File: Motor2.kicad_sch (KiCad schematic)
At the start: 53 parts, among them J601 Step Out, J604 Direction, J605 Direction, Q601 WSF07N10, Q602 WSF07N10, Q603 WSF07N10, Q604 WSF07N10, Q605 WSF07N10, Q606 WSF07N10, Q607 WSF07N10, Q608 WSF07N10

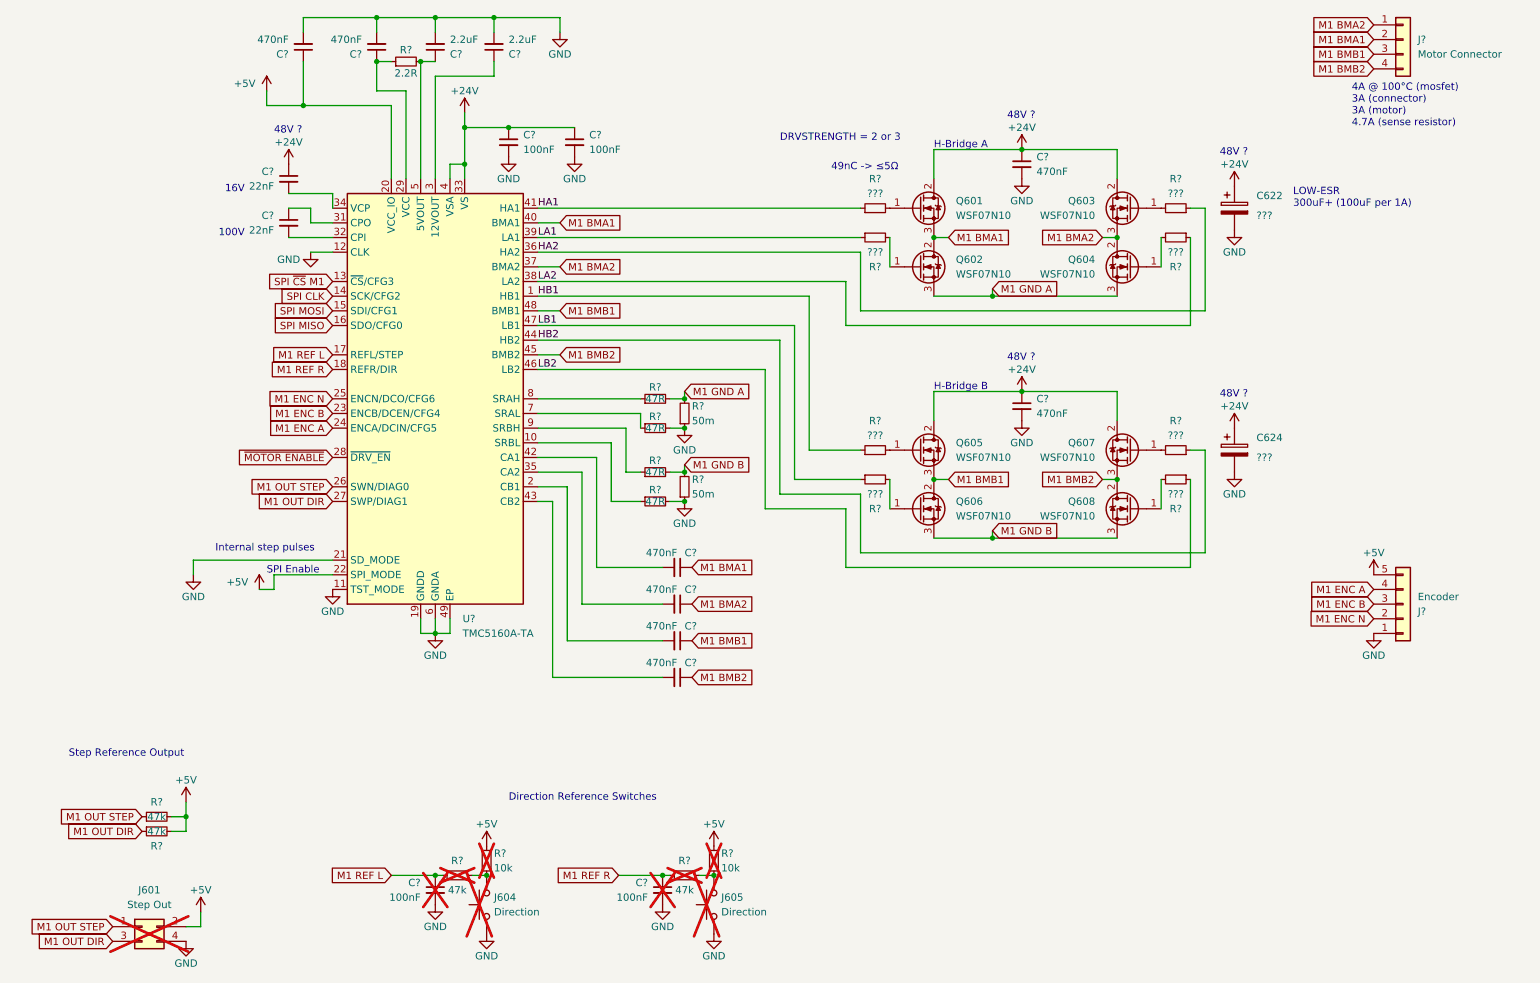
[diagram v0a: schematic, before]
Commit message: Assigning a lot of values to components Change MOSFETS for different (correct) ones Copy Motor1 to Motor2-4 Guess max current per voltage on PowerSupply schema
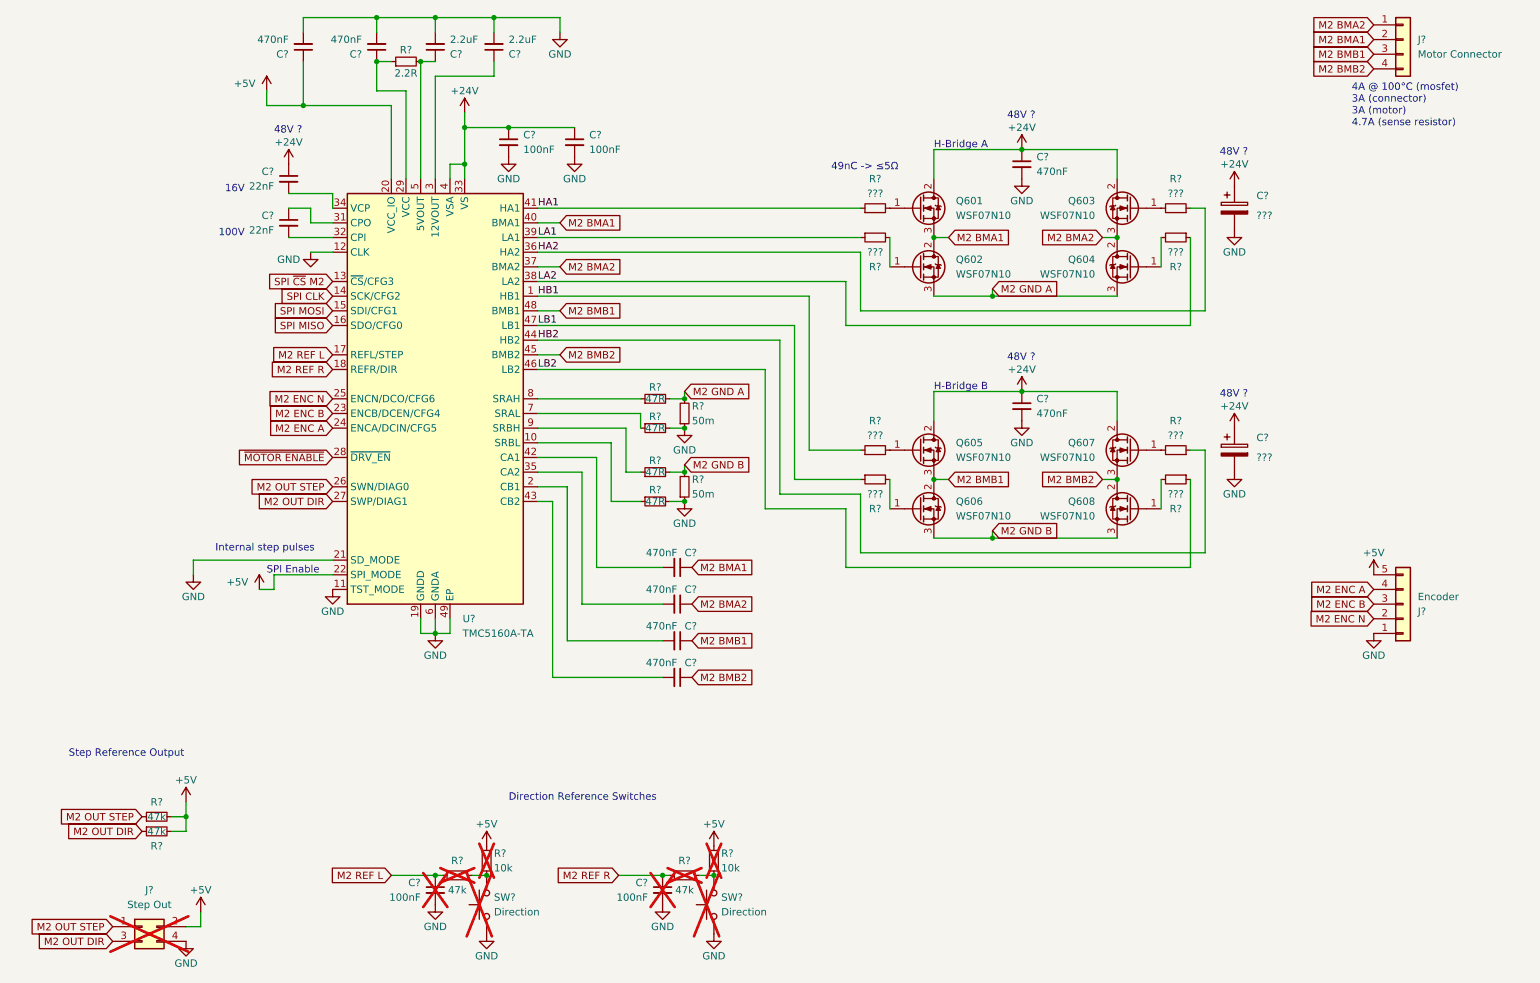
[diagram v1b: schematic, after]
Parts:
- removed C622, C624: ???, symbol Device:C_Polarized
- removed C? (x6): 470nF, Capacitor_SMD:C_1210_3225Metric, symbol Device:C_Small
- removed C? (x4): 100nF, symbol Device:C_Small
- removed C? (x2): 2.2uF, symbol Device:C_Small
- removed C? (x2): 470nF, symbol Device:C_Small
- removed C? (x2): 22nF, symbol Device:C_Small
- removed J601: Step Out, Connector_PinHeader_2.54mm:PinHeader_2x02_P2.54mm_Vertical, symbol Connector_Generic:Conn_02x02_Odd_Even
- removed J604, J605: Direction, Connector_PinHeader_2.54mm:PinHeader_1x02_P2.54mm_Vertical, symbol Switch:SW_Push
- removed J?: Encoder, Connector_JST:JST_XH_B5B-XH-A_1x05_P2.50mm_Vertical, symbol Connector_Generic:Conn_01x05
- removed J?: Motor Connector, Connector_JST:JST_XH_B4B-XH-A_1x04_P2.50mm_Vertical, symbol Connector_Generic:Conn_01x04
- removed R? (x2): 50m, Resistor_SMD:R_2512_6332Metric, symbol Device:R_Small
- removed R? (x4): 47k, symbol Device:R_Small
- removed R? (x8): ???, symbol Device:R_Small
- removed R? (x4): 47R, symbol Device:R_Small
- removed R?: 2.2R, symbol Device:R_Small
- removed R? (x2): 10k, symbol Device:R_Small
- removed U?: TMC5160A-TA, Package_QFP:TQFP-48-1EP_7x7mm_P0.5mm_EP5x5mm_ThermalVias, symbol Driver_Motor:TMC5160A-TA
- added C? (x6): 470nF, Capacitor_SMD:C_1210_3225Metric, symbol Device:C_Small
- added C? (x4): 100nF, symbol Device:C_Small
- added C? (x2): 470nF, symbol Device:C_Small
- added C? (x2): ???, symbol Device:C_Polarized
- added C? (x2): 22nF, symbol Device:C_Small
- added C? (x2): 2.2uF, symbol Device:C_Small
- added J?: Step Out, Connector_PinHeader_2.54mm:PinHeader_2x02_P2.54mm_Vertical, symbol Connector_Generic:Conn_02x02_Odd_Even
- added J?: Motor Connector, Connector_JST:JST_XH_B4B-XH-A_1x04_P2.50mm_Vertical, symbol Connector_Generic:Conn_01x04
- added J?: Encoder, Connector_JST:JST_XH_B5B-XH-A_1x05_P2.50mm_Vertical, symbol Connector_Generic:Conn_01x05
- added R? (x2): 10k, symbol Device:R_Small
- added R? (x4): 47k, symbol Device:R_Small
- added R? (x4): 47R, symbol Device:R_Small
- added R? (x8): ???, symbol Device:R_Small
- added R? (x2): 50m, Resistor_SMD:R_2512_6332Metric, symbol Device:R_Small
- added R?: 2.2R, symbol Device:R_Small
- added SW? (x2): Direction, Connector_PinHeader_2.54mm:PinHeader_1x02_P2.54mm_Vertical, symbol Switch:SW_Push
- added U?: TMC5160A-TA, Package_QFP:TQFP-48-1EP_7x7mm_P0.5mm_EP5x5mm_ThermalVias, symbol Driver_Motor:TMC5160A-TA
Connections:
- net +24V: now also C?.1, C?.1, C?.1, C?.1, C?.1, C?.1, C?.1, U?.33 (VS), U?.4 (VSA)
- net +5V: now also C?.1, J?.2 (Pin_2), J?.5 (Pin_5), R?.2, R?.2, R?.2, R?.2, U?.20 (VCC_IO), U?.22 (SPI_MODE)
- net GND: now also C?.2, C?.2, C?.2, C?.2, C?.2, C?.2, C?.2, C?.2, C?.2, C?.2, C?.2, C?.2, J?.1 (Pin_1), J?.4 (Pin_4), R?.1, R?.1, R?.2, R?.2, SW?.1, SW?.1, U?.11 (TST_MODE), U?.12 (CLK), U?.19 (GNDD), U?.21 (SD_MODE), U?.30 (GNDD), U?.49 (EP), U?.6 (GNDA)
- net HA1: now also R?.1, U?.41 (HA1)
- net HA2: now also R?.1, U?.36 (HA2)
- net HB1: now also R?.1, U?.1 (HB1)
- net HB2: now also R?.1, U?.44 (HB2)
- net LA1: now also R?.1, U?.39 (LA1)
- net LA2: now also R?.1, U?.38 (LA2)
- net LB1: now also R?.1, U?.47 (LB1)
- net LB2: now also R?.1, U?.46 (LB2)
- net SPI CLK: now also U?.14 (SCK/CFG2)
- net SPI MISO: now also U?.16 (SDO/CFG0)
- net SPI MOSI: now also U?.15 (SDI/CFG1)
- net ~{MOTOR ENABLE}: now also U?.28 (~{DRV_EN})
- net at Q606.1 (G): now also R?.2
- net at Q602.1 (G): now also R?.2
- net at Q608.1 (G): now also R?.2
- net at Q601.1 (G): now also R?.2
- net at Q607.1 (G): now also R?.2
- net at Q603.1 (G): now also R?.2
- net at Q605.1 (G): now also R?.2
- net at Q604.1 (G): now also R?.2
- net M1 BMA1 renamed M2 BMA1
- net M2 BMA1: now also C?.1, J?.2 (Pin_2), U?.40 (BMA1)
- net M1 BMA2 renamed M2 BMA2
- net M2 BMA2: now also C?.1, J?.1 (Pin_1), U?.37 (BMA2)
- net M1 BMB1 renamed M2 BMB1
- net M2 BMB1: now also C?.1, J?.3 (Pin_3), U?.48 (BMB1)
- net M1 BMB2 renamed M2 BMB2
- net M2 BMB2: now also C?.1, J?.4 (Pin_4), U?.45 (BMB2)
- net M1 GND A renamed M2 GND A
- net M2 GND A: now also R?.2, R?.2
- net M1 GND B renamed M2 GND B
- net M2 GND B: now also R?.2, R?.2
- new net: R?.1, R?.2, SW?.2 (x2)
- new net: R?.1, U?.7 (SRAL)
- new net: C?.2, U?.42 (CA1)
- new net: C?.2, U?.43 (CB2)
- new net: C?.1, R?.1, U?.29 (VCC)
- new net: C?.1, U?.31 (CPO)
- new net: C?.2, U?.32 (CPI)
- new net: R?.1, U?.9 (SRBH)
- new net: R?.1, U?.10 (SRBL)
- new net: C?.2, U?.2 (CB1)
- new net: C?.1, U?.3 (12VOUT)
- new net: C?.2, U?.34 (VCP)
- new net: C?.2, U?.35 (CA2)
- new net: C?.1, R?.2, U?.5 (5VOUT)
- new net: R?.1, U?.8 (SRAH)
- new net M2 ENC A: J?.4 (Pin_4), U?.24 (ENCA/DCIN/CFG5)
- new net M2 ENC B: J?.3 (Pin_3), U?.23 (ENCB/DCEN/CFG4)
- new net M2 ENC N: J?.2 (Pin_2), U?.25 (ENCN/DCO/CFG6)
- new net M2 OUT DIR: J?.3 (Pin_3), R?.1, U?.27 (SWP/DIAG1)
- new net M2 OUT STEP: J?.1 (Pin_1), R?.1, U?.26 (SWN/DIAG0)
- new net M2 REF L: C?.1, R?.1, U?.17 (REFL/STEP)
- new net M2 REF R: C?.1, R?.1, U?.18 (REFR/DIR)
- new net SPI ~{CS} M2: U?.13 (~{CS}/CFG3)
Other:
- note removed: "DRVSTRENGTH = 2 or 3"
- note removed: "LOW-ESR 300uF+ (100uF per 1A)"
- title: CAN 3D Printer (4 Motor) - Motor 1 -> CAN 3D Printer (4 Motor) - Motor 2

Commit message: Complete schematics Assign every value (very few exceptions) Change TCM5160 from on-board to separate module Add fuses Add power supplies (LDO + 2x buck converter)
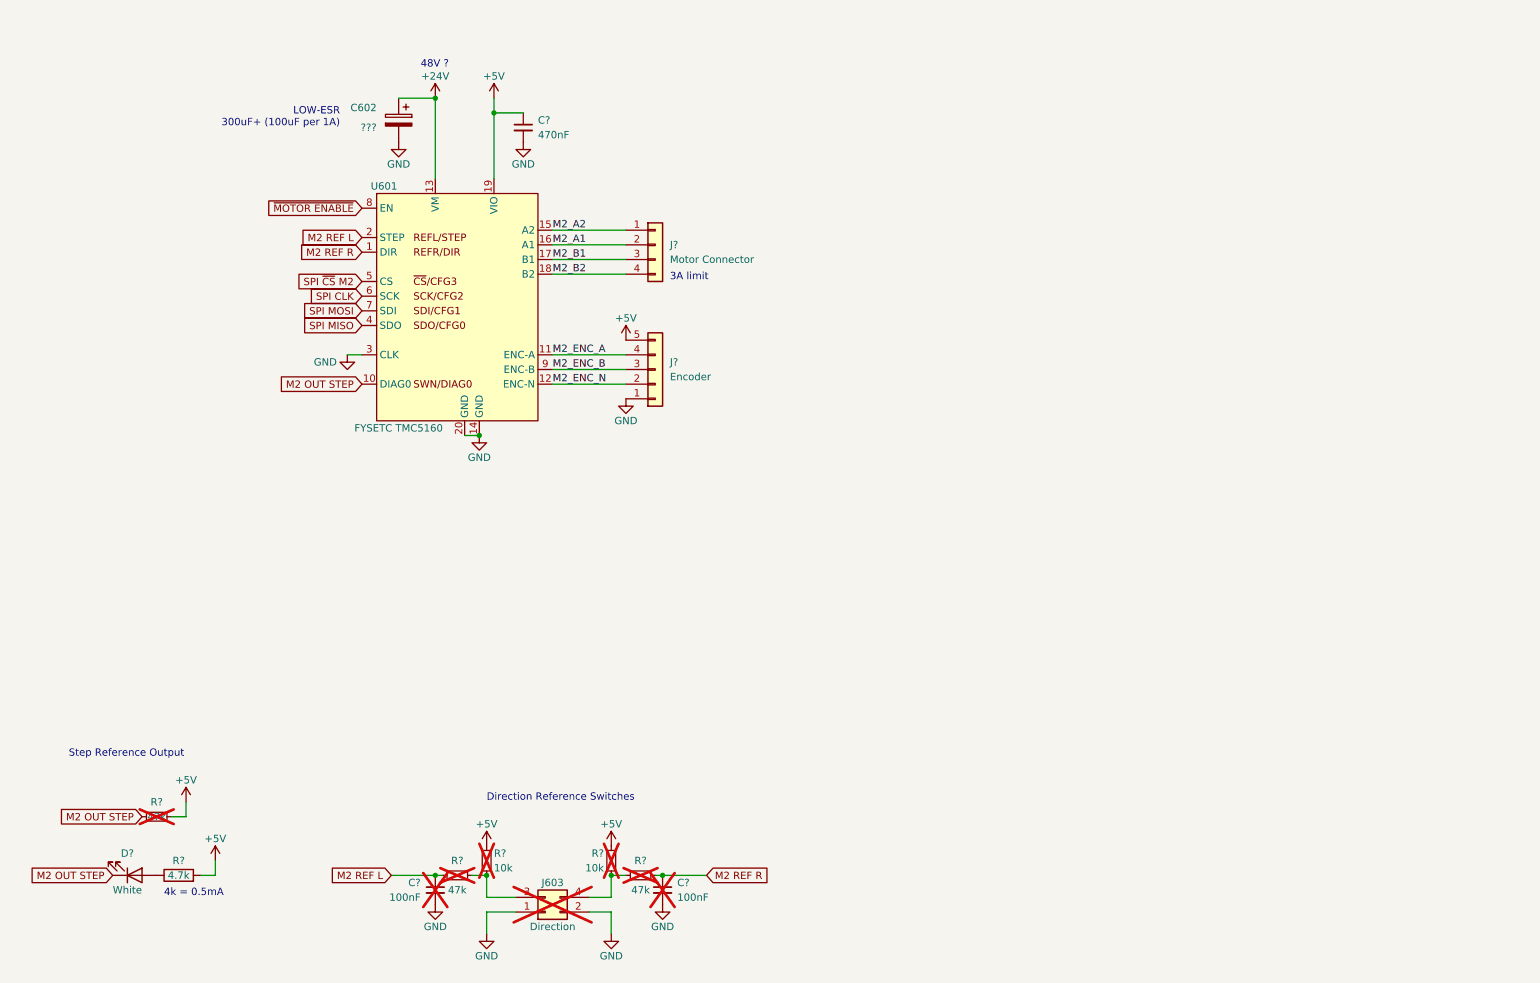
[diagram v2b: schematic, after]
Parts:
- removed C? (x6): 470nF, Capacitor_SMD:C_1210_3225Metric, symbol Device:C_Small
- removed C? (x4): 100nF, symbol Device:C_Small
- removed C? (x2): 470nF, symbol Device:C_Small
- removed C? (x2): ???, symbol Device:C_Polarized
- removed C? (x2): 22nF, symbol Device:C_Small
- removed C? (x2): 2.2uF, symbol Device:C_Small
- removed J?: Step Out, Connector_PinHeader_2.54mm:PinHeader_2x02_P2.54mm_Vertical, symbol Connector_Generic:Conn_02x02_Odd_Even
- removed J?: Motor Connector, Connector_JST:JST_XH_B4B-XH-A_1x04_P2.50mm_Vertical, symbol Connector_Generic:Conn_01x04
- removed J?: Encoder, Connector_JST:JST_XH_B5B-XH-A_1x05_P2.50mm_Vertical, symbol Connector_Generic:Conn_01x05
- removed Q601, Q602, Q603, Q604, Q605, Q606, Q607, Q608: WSF07N10, Package_TO_SOT_SMD:TO-252-2, symbol Transistor_FET:QM6006D
- removed R? (x2): 10k, symbol Device:R_Small
- removed R? (x4): 47k, symbol Device:R_Small
- removed R? (x4): 47R, symbol Device:R_Small
- removed R? (x8): ???, symbol Device:R_Small
- removed R? (x2): 50m, Resistor_SMD:R_2512_6332Metric, symbol Device:R_Small
- removed R?: 2.2R, symbol Device:R_Small
- removed SW? (x2): Direction, Connector_PinHeader_2.54mm:PinHeader_1x02_P2.54mm_Vertical, symbol Switch:SW_Push
- removed U?: TMC5160A-TA, Package_QFP:TQFP-48-1EP_7x7mm_P0.5mm_EP5x5mm_ThermalVias, symbol Driver_Motor:TMC5160A-TA
- added C602: ???, symbol Device:C_Polarized
- added C? (x2): 100nF, Capacitor_SMD:C_0402_1005Metric, symbol Device:C_Small
- added C?: 470nF, Capacitor_SMD:C_0603_1608Metric, symbol Device:C_Small
- added D?: White, LED_SMD:LED_0402_1005Metric, symbol Device:LED
- added J603: Direction, Connector_PinHeader_2.54mm:PinHeader_2x02_P2.54mm_Vertical, symbol Connector_Generic:Conn_02x02_Odd_Even
- added J?: Encoder, Connector_JST:JST_XH_B5B-XH-A_1x05_P2.50mm_Vertical, symbol Connector_Generic:Conn_01x05
- added J?: Motor Connector, Connector_JST:JST_XH_B4B-XH-A_1x04_P2.50mm_Vertical, symbol Connector_Generic:Conn_01x04
- added R? (x2): 10k, Resistor_SMD:R_0603_1608Metric, symbol Device:R_Small
- added R? (x3): 47k, Resistor_SMD:R_0603_1608Metric, symbol Device:R_Small
- added R?: 4.7k, Resistor_SMD:R_0603_1608Metric, symbol Device:R
- added U601: FYSETC TMC5160, Custom:FYSETC TMC5160, symbol Custom:FYSETC_TMC5160
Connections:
- net +24V: now also C602.1, U601.13 (VM)
- net +5V: now also C?.1, J?.5 (Pin_5), R?.2, R?.2, R?.2, R?.2, U601.19 (VIO)
- net GND: now also C602.2, C?.2, C?.2, C?.2, J603.1 (Pin_1), J603.2 (Pin_2), J?.1 (Pin_1), U601.14 (GND), U601.20 (GND), U601.3 (CLK)
- net M2 OUT STEP: now also D?.1 (K), R?.1, U601.10 (DIAG0)
- net M2 REF L: now also C?.1, R?.1, U601.2 (STEP)
- net M2 REF R: now also C?.1, R?.1, U601.1 (DIR)
- net SPI CLK: now also U601.6 (SCK)
- net SPI MISO: now also U601.4 (SDO)
- net SPI MOSI: now also U601.7 (SDI)
- net SPI ~{CS} M2: now also U601.5 (CS)
- net ~{MOTOR ENABLE}: now also U601.8 (EN)
- new net: J603.3 (Pin_3), R?.1, R?.2
- new net: J603.4 (Pin_4), R?.1, R?.2
- new net: D?.2 (A), R?.1
- new net M2_A1: J?.2 (Pin_2), U601.16 (A1)
- new net M2_A2: J?.1 (Pin_1), U601.15 (A2)
- new net M2_B1: J?.3 (Pin_3), U601.17 (B1)
- new net M2_B2: J?.4 (Pin_4), U601.18 (B2)
- new net M2_ENC_A: J?.4 (Pin_4), U601.11 (ENC-A)
- new net M2_ENC_B: J?.3 (Pin_3), U601.9 (ENC-B)
- new net M2_ENC_N: J?.2 (Pin_2), U601.12 (ENC-N)
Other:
- note added: "3A limit"
- note added: "4k = 0.5mA"
- note added: "LOW-ESR 300uF+ (100uF per 1A)"
- note removed: "100V"
- note removed: "16V"
- note removed: "49nC -> ≤5Ω"
- note removed: "4A @ 100°C (mosfet) 3A (connector) 3A (motor) 4.7A (sense resistor)"
- note removed: "H-Bridge A"
- note removed: "H-Bridge B"
- note removed: "Internal step pulses"
- note removed: "SPI Enable"

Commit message: More PCB placement, fix 48V for Motors
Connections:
- net +24V renamed +48V
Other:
- note removed: "48V ?"
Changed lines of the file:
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@@
     (company "Abit Gray")
   )
+  (junction (at 91.44 39.37) (diameter 0) (color 0 0 0 0)
+  )
   (junction (at 121.92 173.99) (diameter 0) (color 0 0 0 0)
   )
@@
   (junction (at 101.6 41.91) (diameter 0) (color 0 0 0 0)
   )
-  (junction (at 91.44 39.37) (diameter 0) (color 0 0 0 0)
-  )
   (wire (pts (xy 118.11 180.34) (xy 121.92 180.34))
     (stroke (width 0) (type default))
@@
   (wire (pts (xy 53.34 173.99) (xy 50.8 173.99))
     (stroke (width 0) (type default))
-  )
-  (text "48V ?" (at 88.9 34.29 0)
-    (effects (font (size 1.27 1.27)) (justify left bottom))
   )
   (text "Step Reference Output" (at 27.94 153.67 0)
@@
     )
   )
+  (symbol (lib_id "power:+48V") (at 91.44 39.37 0) (unit 1)
+    (in_bom yes) (on_board yes) (dnp no)
+    (property "Reference" "#PWR0204" (at 91.44 43.18 0)
+      (effects (font (size 1.27 1.27)) hide)
+    )
+    (property "Value" "+48V" (at 91.44 35.56 0)
+      (effects (font (size 1.27 1.27)))
+    )
+    (property "Footprint" "" (at 91.44 39.37 0)
+      (effects (font (size 1.27 1.27)) hide)
+    )
+    (property "Datasheet" "" (at 91.44 39.37 0)
+      (effects (font (size 1.27 1.27)) hide)
+    )
+    (pin "1")
+    (instances
+      (project "Can3DPrinter4Motor"
+        (path "/cb4e159a-5c17-494a-ba7f-10e700f814f1/e05e1111-b676-4692-8151-4de155805267"
+          (reference "#PWR0204") (unit 1)
+        )
+        (path "/cb4e159a-5c17-494a-ba7f-10e700f814f1"
+          (reference "#PWR0113") (unit 1)
+        )
+        (path "/cb4e159a-5c17-494a-ba7f-10e700f814f1/03ab3e80-f454-40c8-8f97-43a0b791de0b/c731393f-82c9-42eb-b1cc-cc38a32cf9d8"
+          (reference "#PWR0701") (unit 1)
+        )
+      )
+    )
+  )
   (symbol (lib_id "power:GND") (at 76.2 83.82 0) (unit 1)
     (in_bom yes) (on_board yes) (dnp no)
@@
         )
       )
-    )
-  )
-  (symbol (lib_id "power:+24V") (at 91.44 39.37 0) (unit 1)
-    (in_bom yes) (on_board yes) (dnp no)
-    (property "Reference" "#PWR?" (at 91.44 43.18 0)
-      (effects (font (size 1.27 1.27)) hide)
-    )
-    (property "Value" "+24V" (at 91.44 35.56 0)
-      (effects (font (size 1.27 1.27)))
-    )
-    (property "Footprint" "" (at 91.44 39.37 0)
-      (effects (font (size 1.27 1.27)) hide)
-    )
-    (property "Datasheet" "" (at 91.44 39.37 0)
-      (effects (font (size 1.27 1.27)) hide)
-    )
-    (pin "1")
-    (instances
-      (project "Can3DPrinter4Motor"
-        (path "/cb4e159a-5c17-494a-ba7f-10e700f814f1/03ab3e80-f454-40c8-8f97-43a0b791de0b"
-          (reference "#PWR?") (unit 1)
-        )
-        (path "/cb4e159a-5c17-494a-ba7f-10e700f814f1/03ab3e80-f454-40c8-8f97-43a0b791de0b/a3514610-4e2d-47ba-84b8-39806e951746"
-          (reference "#PWR0635") (unit 1)
-        )
-        (path "/cb4e159a-5c17-494a-ba7f-10e700f814f1/03ab3e80-f454-40c8-8f97-43a0b791de0b/c731393f-82c9-42eb-b1cc-cc38a32cf9d8"
-          (reference "#PWR0705") (unit 1)
-        )
-        (path "/cb4e159a-5c17-494a-ba7f-10e700f814f1/03ab3e80-f454-40c8-8f97-43a0b791de0b/596394bf-80ea-4be7-ad96-94dd67657b85"
-          (reference "#PWR0805") (unit 1)
-        )
-        (path "/cb4e159a-5c17-494a-ba7f-10e700f814f1/03ab3e80-f454-40c8-8f97-43a0b791de0b/47aa3abf-8d06-4c45-872c-33ec1f9a6564"
-          (reference "#PWR0905") (unit 1)
-        )
-      )
